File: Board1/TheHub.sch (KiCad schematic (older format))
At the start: 53 parts, among them J1 ARM_ADC_1, J10 SCIENCE + WHEELS POWER CONN, J11 RFD900, J12 I2C_1 Test Point, J13 I2C_2 Test Point, J14 CONN_02X15, J15 GPIO Test, J16 I2C_3 Test Point, J17 12V OUT, J18 7.4V IN, J19 ANALOG SENSORS, J2 ARM_ADC_2, J20 GPS, J21 COMPASS, J3 ARM_PWM_OUT, J4 ARM POWER CONN, J5 NucleoF411RE, J6 SCI_ADC_1, J7 SCIENCE_PWM_OUT, J8 12V MAIN POWER, J9 WHEEL_ADC_1, U1 PRE-PCA9685, U2 PRE-ADS1115, U3 PRE-ADS1115, U4 PRE-PCA9685, U5 PRE-ADS1115, U6 LD1086DT33TR, U7 LM340MP-5.0, U9 PRE-ADS1115

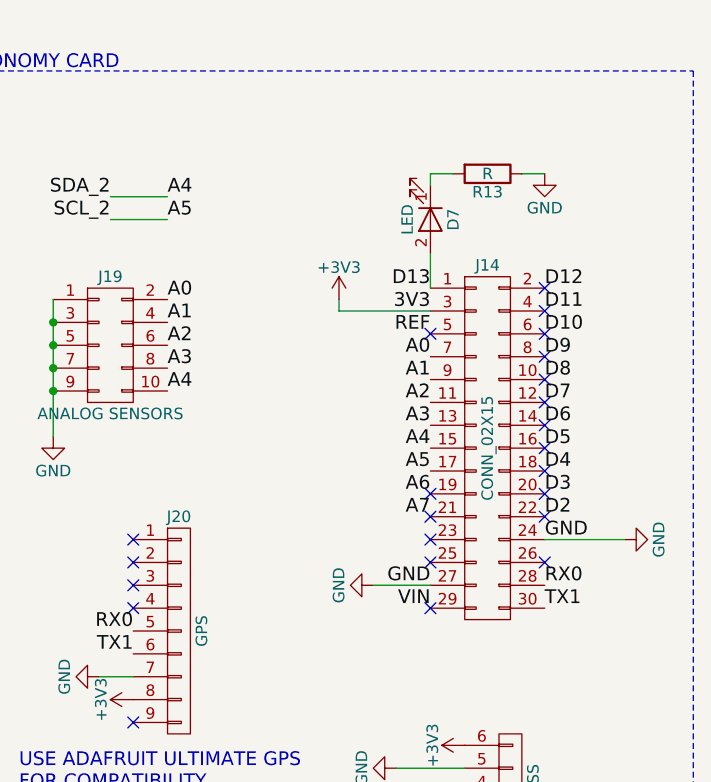
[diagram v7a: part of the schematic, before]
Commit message: Create cvpcb assiciation, generate netlist
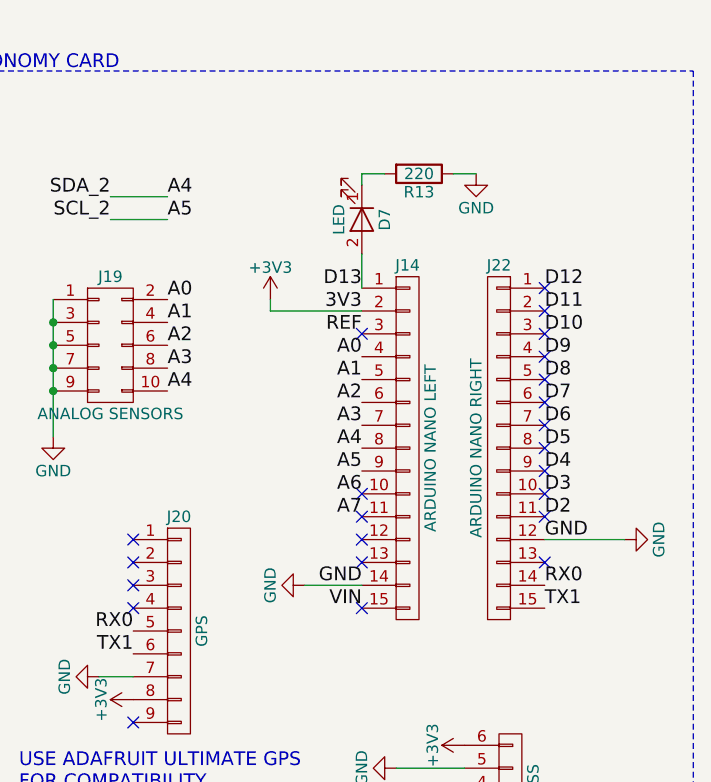
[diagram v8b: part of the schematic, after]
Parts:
- removed J14: CONN_02X15, symbol CONN_02X15
- added J14: ARDUINO NANO LEFT, Pin_Headers:Pin_Header_Straight_1x15_Pitch2.54mm, symbol CONN_01X15
- added J22: ARDUINO NANO RIGHT, Pin_Headers:Pin_Header_Straight_1x15_Pitch2.54mm, symbol CONN_01X15
- C1, C2, C3, C4: footprint (none) -> Capacitors_SMD:C_0805
- D1, D2, D3, D4, D5, D6, D7: footprint (none) -> LEDs:LED_0805
- J1, J2, J6, J9: footprint (none) -> Pin_Headers:Pin_Header_Straight_2x04_Pitch2.54mm
- J10, J5: footprint (none) -> Pin_Headers:Pin_Header_Straight_2x19_Pitch2.54mm
- J11: footprint (none) -> Pin_Headers:Pin_Header_Straight_2x08_Pitch2.54mm
- J12, J13, J16: footprint (none) -> Pin_Headers:Pin_Header_Straight_1x03_Pitch2.54mm
- J15: footprint (none) -> Pin_Headers:Pin_Header_Straight_1x04_Pitch2.54mm
- J17, J18, J8: footprint (none) -> FoxWestern:XT60
- J19: footprint (none) -> Pin_Headers:Pin_Header_Straight_2x05_Pitch2.54mm
- J20: footprint (none) -> Pin_Headers:Pin_Header_Straight_1x09_Pitch2.54mm
- J21: footprint (none) -> Pin_Headers:Pin_Header_Straight_1x06_Pitch2.54mm
- J3, J7: footprint (none) -> Pin_Headers:Pin_Header_Straight_1x16_Pitch2.54mm
- J4: footprint (none) -> Pin_Headers:Pin_Header_Straight_2x16_Pitch2.54mm
- R1, R2, R6, R7, R8, R9: footprint (none) -> Resistors_SMD:R_0805
- R13: value R -> 220
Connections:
- net +3V3: now also J14.2 (P2)
- net A0: now also J14.4 (P4)
- net A1: now also J14.5 (P5)
- net A2: now also J14.6 (P6)
- net A3: now also J14.7 (P7)
- net A4: now also J14.8 (P8)
- net A5: now also J14.9 (P9)
- net A6: now also J14.10 (P10)
- net A7: now also J14.11 (P11)
- net D10: now also J22.3 (P3)
- net D11: now also J22.2 (P2)
- net D12: now also J22.1 (P1)
- net D13: now also J14.1 (P1)
- net D2: now also J22.11 (P11)
- net D3: now also J22.10 (P10)
- net D4: now also J22.9 (P9)
- net D5: now also J22.8 (P8)
- net D6: now also J22.7 (P7)
- net D7: now also J22.6 (P6)
- net D8: now also J22.5 (P5)
- net D9: now also J22.4 (P4)
- net GND: now also J14.14 (P14), J22.12 (P12)
- net REF: now also J14.3 (P3)
- net RX0: now also J22.14 (P14)
- net TX1: now also J22.15 (P15)
- net VIN: now also J14.15 (P15)
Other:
- moved on the sheet: D7, R13
